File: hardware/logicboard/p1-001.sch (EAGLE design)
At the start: 23 parts, among them IC1 74LS07N, U1 TLC5940-NT, X1 HIROSE-DX10LM1-14SE

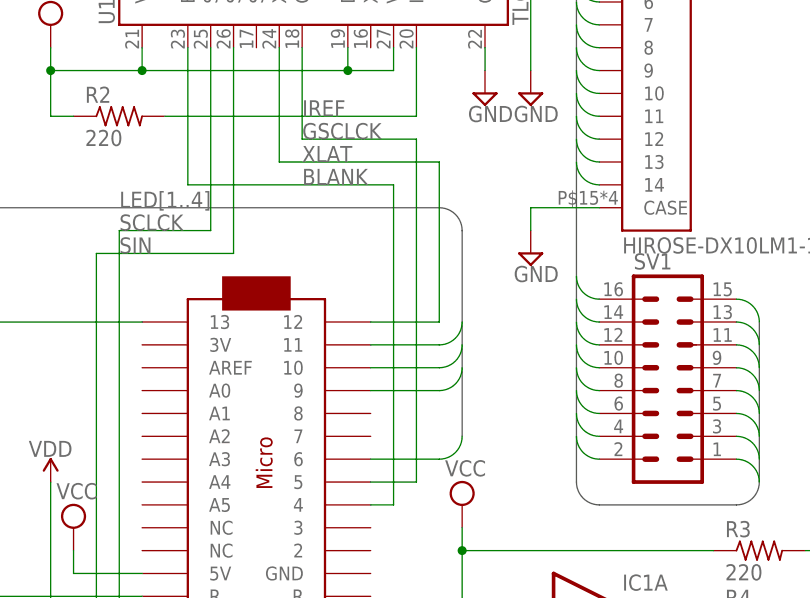
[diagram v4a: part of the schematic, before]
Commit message: Swapped pin D7 and D12.
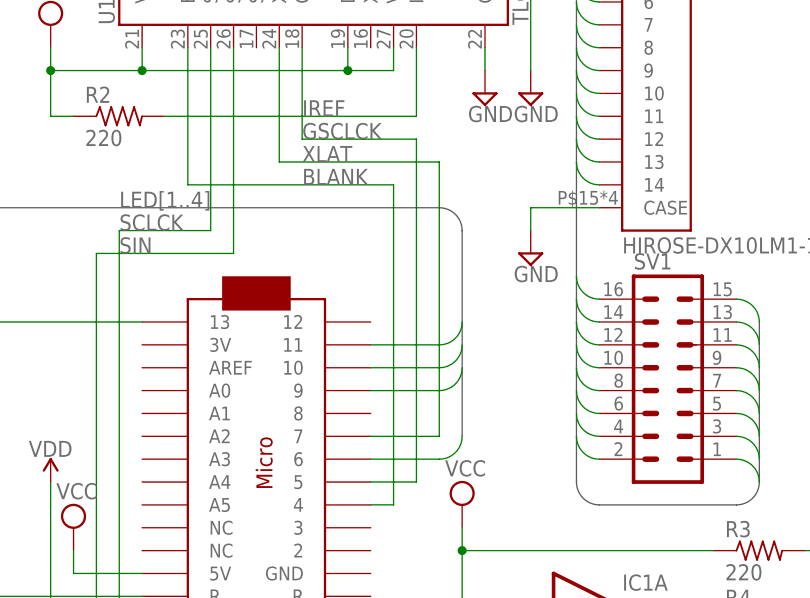
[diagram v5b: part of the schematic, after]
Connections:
- net XLAT: now also U$1.7; no longer U$1.12
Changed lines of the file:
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@@
 <wire x1="91.44" y1="88.9" x2="73.66" y2="88.9" width="0.1524" layer="91"/>
 <label x="76.2" y="88.9" size="1.778" layer="95"/>
-<wire x1="83.82" y1="71.12" x2="91.44" y2="71.12" width="0.1524" layer="91"/>
-<wire x1="91.44" y1="71.12" x2="91.44" y2="88.9" width="0.1524" layer="91"/>
-<pinref part="U$1" gate="G$1" pin="12"/>
+<wire x1="91.44" y1="58.42" x2="91.44" y2="88.9" width="0.1524" layer="91"/>
+<pinref part="U$1" gate="G$1" pin="7"/>
+<wire x1="91.44" y1="58.42" x2="83.82" y2="58.42" width="0.1524" layer="91"/>
 </segment>
 </net>

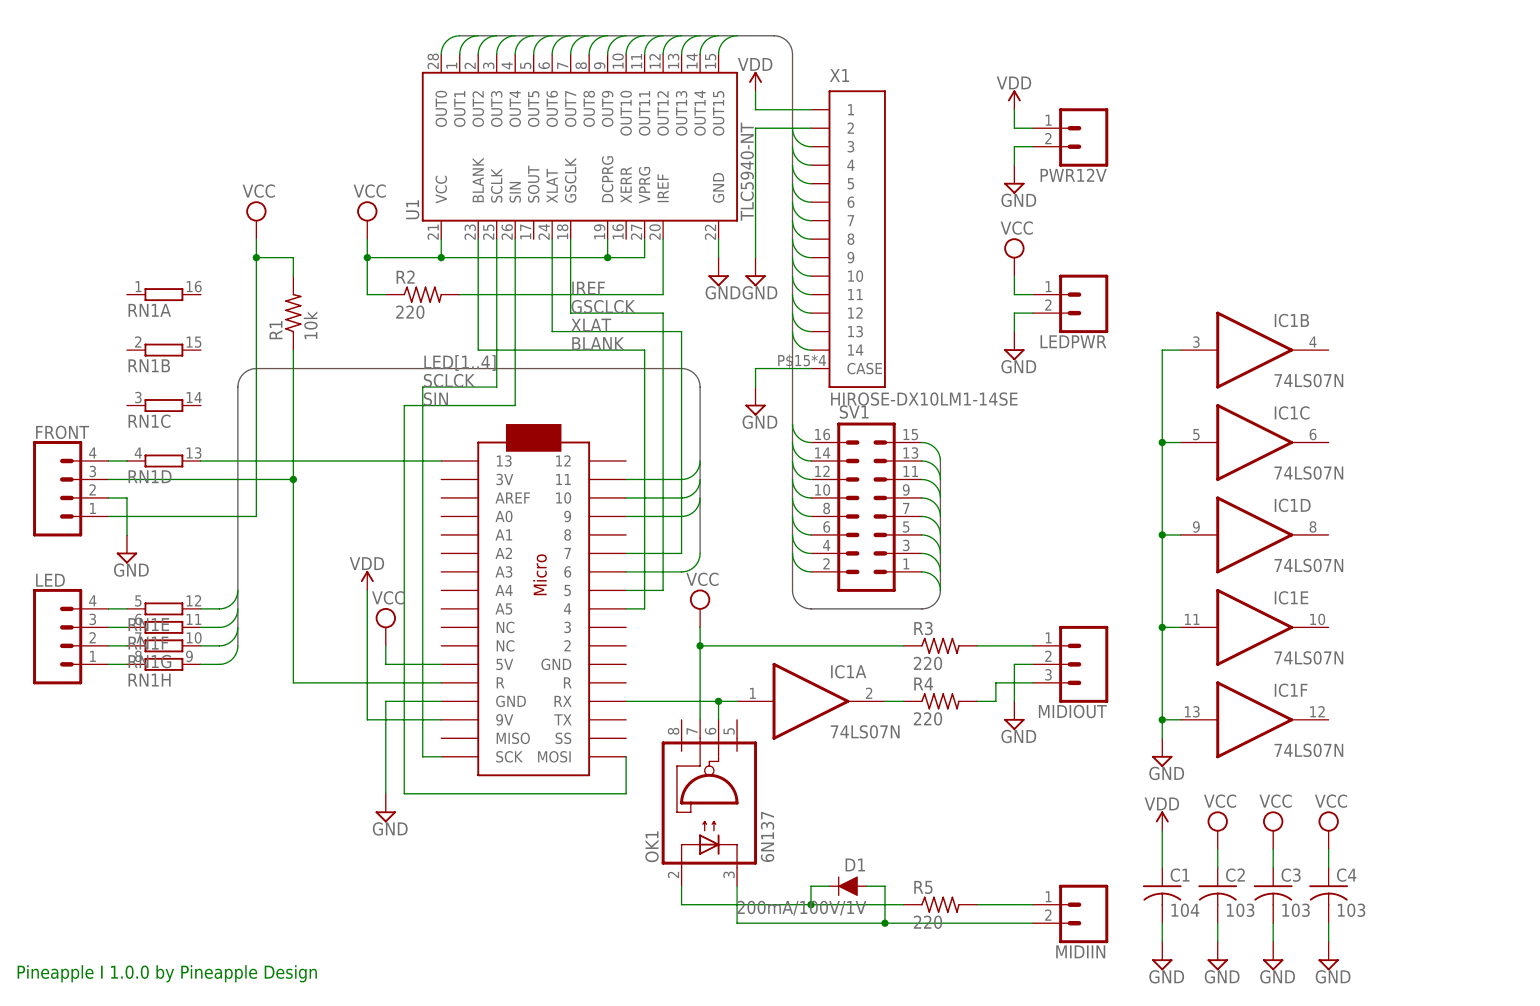
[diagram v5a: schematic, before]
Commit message: 1-Wire ROM.
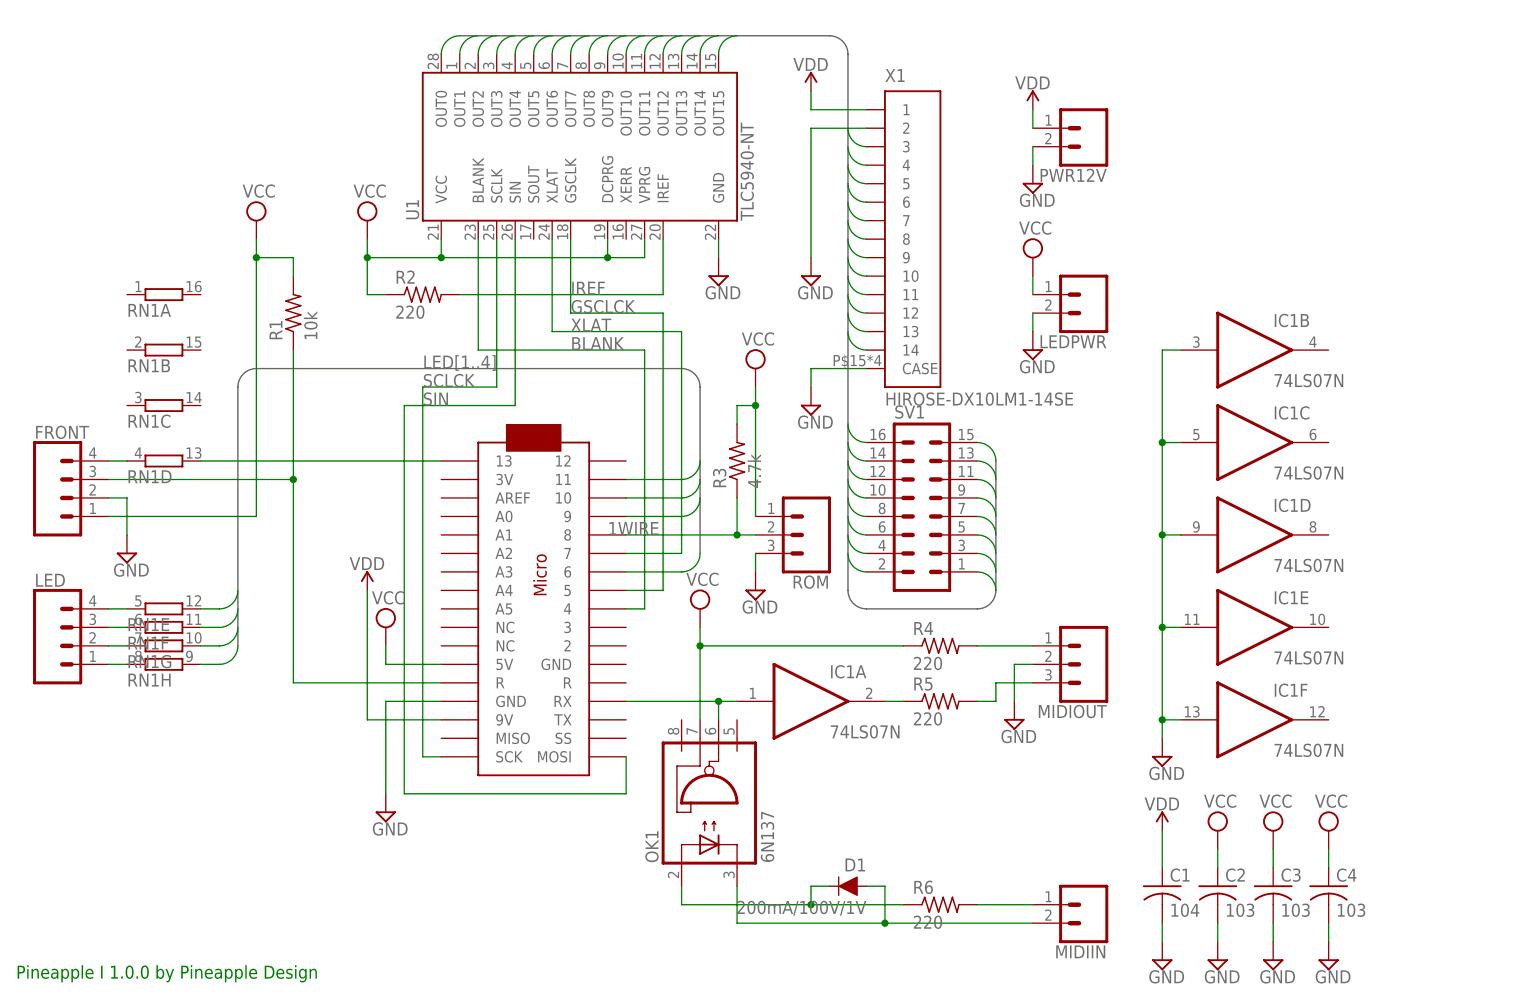
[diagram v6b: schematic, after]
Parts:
- added R6: 220, resistor:R-US_0204/5
- added ROM: (no value), SparkFun-Connectors:CONN_03JST-PTH-VERT
- R3: value 220 -> 4.7k
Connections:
- new net 1WIRE: R3.1, ROM.2, U$1.8
- net GND: now also ROM.3
- net MIDITX-: now also R5.2; no longer R4.2
- net N$2: now also R5.1; no longer R4.1
- net N$4: now also R4.2; no longer R3.2
- net N$5: now also R6.1; no longer R5.1
- net N$6: now also R6.2; no longer R5.2
- net VCC: now also R3.2, R4.1, ROM.1; no longer R3.1
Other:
- moved on the sheet: R3, R4, R5, SV1, X1

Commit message: Relay.
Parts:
- added D2: 200mA/100V/1V, SparkFun-DiscreteSemi:DIODE-1N4148
- added I2C: (no value), pinhead:PINHD-1X4
- added K1: G5V1, relay:G5V1
- added R7: 3.3k, resistor:R-US_0204/5
- added RELAY: (no value), SparkFun-Connectors:CONN_02JST-PTH-2
- added T1: 2SC1815, transistor:2SC1815
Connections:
- new net I2C1: I2C.3, U$1.2
- new net I2C2: I2C.4, U$1.3
- new net N$14: R7.1, U$1.12
- new net N$15: R7.2, T1.B
- new net N$16: D2.A, K11.2, T1.C
- new net N$17: K12.S, RELAY.1
- new net N$18: K12.P, K12.P@1, RELAY.2
- net GND: now also I2C.2, T1.E, U$1.GND@1
- net GSCLCK: now also U$1.6; no longer U$1.5
- net LED1: now also U$1.5; no longer U$1.6
- net VCC: now also D2.C, I2C.1, K11.1
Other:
- moved on the sheet: LEDPWR, PWR12V, X1

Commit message: Fixed small errors.
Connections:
- net GND: now also RN1A.1, RN1A.2, RN1B.1, RN1B.2, RN1C.1, RN1C.2
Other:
- moved on the sheet: RN1A, RN1B, RN1C
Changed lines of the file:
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@@
 <part name="K1" library="relay" library_urn="urn:adsk.eagle:library:339" deviceset="G5V1" device="" package3d_urn="urn:adsk.eagle:package:24341/1"/>
 <part name="RELAY" library="SparkFun-Connectors" deviceset="CONN_02" device="JST-PTH-2"/>
+<part name="SUPPLY32" library="supply2" library_urn="urn:adsk.eagle:library:372" deviceset="GND" device=""/>
 </parts>
 <sheets>
@@
 <instance part="R2" gate="G$1" x="55.88" y="93.98"/>
 <instance part="LED" gate="G$1" x="7.62" y="45.72"/>
-<instance part="RN1" gate="A" x="20.32" y="93.98"/>
-<instance part="RN1" gate="B" x="20.32" y="86.36"/>
-<instance part="RN1" gate="C" x="20.32" y="78.74"/>
+<instance part="RN1" gate="A" x="195.58" y="20.32"/>
+<instance part="RN1" gate="B" x="195.58" y="15.24"/>
+<instance part="RN1" gate="C" x="195.58" y="10.16"/>
 <instance part="RN1" gate="D" x="20.32" y="71.12"/>
 <instance part="RN1" gate="E" x="20.32" y="50.8"/>
@@
 <instance part="K1" gate="2" x="154.94" y="106.68"/>
 <instance part="RELAY" gate="G$1" x="152.4" y="127" rot="R270"/>
+<instance part="SUPPLY32" gate="GND" x="203.2" y="2.54"/>
 </instances>
 <busses>
@@
 <wire x1="139.7" y1="88.9" x2="139.7" y2="91.44" width="0.1524" layer="91"/>
 </segment>
+<segment>
+<pinref part="RN1" gate="A" pin="1"/>
+<wire x1="190.5" y1="20.32" x2="187.96" y2="20.32" width="0.1524" layer="91"/>
+<wire x1="187.96" y1="20.32" x2="187.96" y2="15.24" width="0.1524" layer="91"/>
+<pinref part="RN1" gate="B" pin="1"/>
+<wire x1="187.96" y1="15.24" x2="190.5" y2="15.24" width="0.1524" layer="91"/>
+<wire x1="187.96" y1="15.24" x2="187.96" y2="10.16" width="0.1524" layer="91"/>
+<junction x="187.96" y="15.24"/>
+<pinref part="RN1" gate="C" pin="1"/>
+<wire x1="187.96" y1="10.16" x2="190.5" y2="10.16" width="0.1524" layer="91"/>
+<wire x1="187.96" y1="10.16" x2="187.96" y2="5.08" width="0.1524" layer="91"/>
+<junction x="187.96" y="10.16"/>
+<wire x1="187.96" y1="5.08" x2="203.2" y2="5.08" width="0.1524" layer="91"/>
+<pinref part="RN1" gate="A" pin="2"/>
+<wire x1="200.66" y1="20.32" x2="203.2" y2="20.32" width="0.1524" layer="91"/>
+<pinref part="RN1" gate="B" pin="2"/>
+<wire x1="203.2" y1="20.32" x2="203.2" y2="15.24" width="0.1524" layer="91"/>
+<wire x1="203.2" y1="15.24" x2="200.66" y2="15.24" width="0.1524" layer="91"/>
+<pinref part="RN1" gate="C" pin="2"/>
+<wire x1="200.66" y1="10.16" x2="203.2" y2="10.16" width="0.1524" layer="91"/>
+<wire x1="203.2" y1="10.16" x2="203.2" y2="15.24" width="0.1524" layer="91"/>
+<junction x="203.2" y="15.24"/>
+<wire x1="203.2" y1="5.08" x2="203.2" y2="10.16" width="0.1524" layer="91"/>
+<junction x="203.2" y="10.16"/>
+<pinref part="SUPPLY32" gate="GND" pin="GND"/>
+<junction x="203.2" y="5.08"/>
+</segment>
 </net>
